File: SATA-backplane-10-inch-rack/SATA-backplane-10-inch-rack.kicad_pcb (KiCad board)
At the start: 2 copper layers, 210.1 x 69.6 mm, 38 parts, among them J101 Conn_01x06, J201 67800-5001, J202 1735284-2, J301 67800-5001, J302 1735284-2, J401 67800-5001, J402 1735284-2, J501 67800-5001, J502 1735284-2, J601 67800-5001, J602 1735284-2, J701 67800-5001, J702 1735284-2, Q101 DMG1012UW, Q102 DMG1012UW, U1 NCP1117-3.3_SOT223

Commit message: Add final silkscreen items
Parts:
- added REF**: WEEE-Logo_5.6x8mm_SilkScreen, Symbol:WEEE-Logo_5.6x8mm_SilkScreen, F.Cu at (37.8, 158.0)
- added REF**: ESD-Logo_8.9x8mm_SilkScreen, Symbol:ESD-Logo_8.9x8mm_SilkScreen, F.Cu at (49.8, 157.9)
- added REF**: KiCad-Logo2_6mm_SilkScreen, Symbol:KiCad-Logo2_6mm_SilkScreen, F.Cu at (68.0, 157.9)
- added REF**: Symbol_CreativeCommonsPublicDomain_SilkScreenTop_Small, Symbol:Symbol_CreativeCommonsPublicDomain_SilkScreenTop_Small, F.Cu at (200.7, 156.5)
- added REF**: OSHW-Logo2_9.8x8mm_SilkScreen, Symbol:OSHW-Logo2_9.8x8mm_SilkScreen, F.Cu at (86.2, 158.8)
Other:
- board text added: "- +"
- board text added: "ACTIVITY LED"
- board text added: "Note: Not all disk drives require all power rails to be present, however the On-board +3V3 power supply requires +5V present. Check the power requirements of your disk drives before connecting"
- board text added: "github.com/labitat/SATA-backplane-10-inch-rack"
- board text added: "{dblquote}Send More Memes{dblquote}"
- board text removed: "ACT"

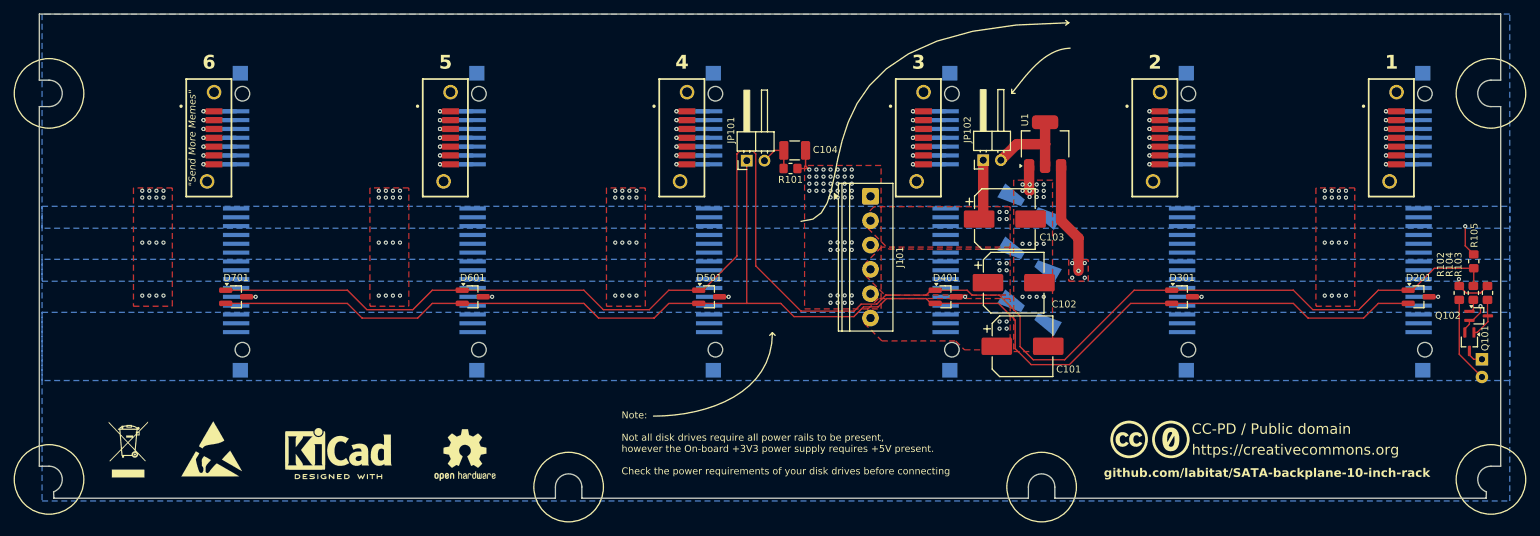
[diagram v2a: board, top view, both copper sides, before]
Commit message: Rearrange reference designators numbering and silkscreen items
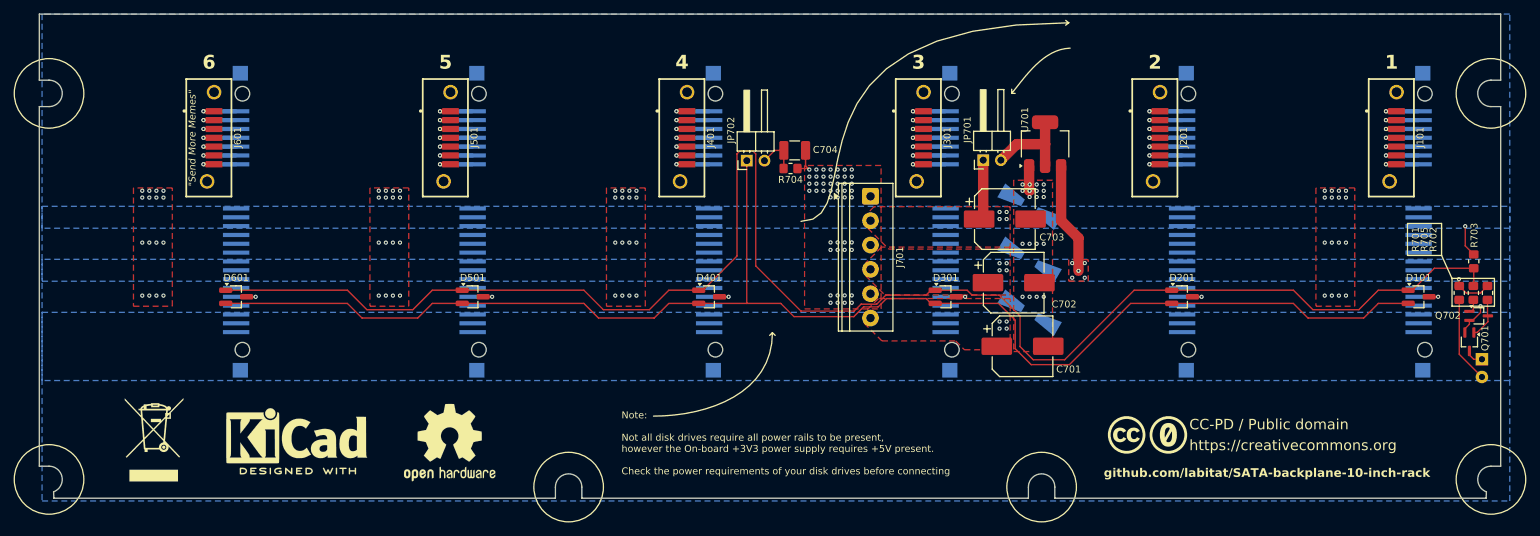
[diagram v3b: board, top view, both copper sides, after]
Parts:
- removed REF**: WEEE-Logo_5.6x8mm_SilkScreen, Symbol:WEEE-Logo_5.6x8mm_SilkScreen
- removed REF**: ESD-Logo_8.9x8mm_SilkScreen, Symbol:ESD-Logo_8.9x8mm_SilkScreen
- removed REF**: KiCad-Logo2_6mm_SilkScreen, Symbol:KiCad-Logo2_6mm_SilkScreen
- removed REF**: Symbol_CreativeCommonsPublicDomain_SilkScreenTop_Small, Symbol:Symbol_CreativeCommonsPublicDomain_SilkScreenTop_Small
- removed REF**: OSHW-Logo2_9.8x8mm_SilkScreen, Symbol:OSHW-Logo2_9.8x8mm_SilkScreen
- added SYM701: ~, Symbol:Symbol_CreativeCommonsPublicDomain_SilkScreenTop_Small, F.Cu at (200.3, 155.9)
- added SYM702: ~, Symbol:WEEE-Logo_8.4x12mm_SilkScreen, F.Cu at (41.5, 156.6)
- added SYM704: ~, Symbol:OSHW-Logo2_14.6x12mm_SilkScreen, F.Cu at (84.0, 157.0)
- added SYM705: ~, Symbol:KiCad-Logo2_8mm_SilkScreen, F.Cu at (62.0, 156.0)
- U701: renamed from U1; value NCP1117-3.3_SOT223 -> LDI1117-3.3H
- renumbered C101 to C701, C102 to C702, C103 to C703, C104 to C704, D201 to D101, D301 to D201, D401 to D301, D501 to D401, D601 to D501, D701 to D601, D101 to D701, D102 to D702, D103 to D703, D104 to D704, J201 to J101, J202 to J102, J301 to J201, J302 to J202, J401 to J301, J402 to J302, J501 to J401, J502 to J402, J601 to J501, J602 to J502, J701 to J601, J702 to J602, J101 to J701, JP102 to JP701, JP101 to JP702, Q101 to Q701, Q102 to Q702, R102 to R701, R103 to R702, R105 to R703, R101 to R704, R104 to R705
